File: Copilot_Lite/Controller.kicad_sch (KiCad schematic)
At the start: 36 parts, among them J11 SERIAL_MODE, J12 SERIAL_VOLTAGE_SELECT, Q5 BSS138, Q6 BSS138, Q7 BSS138, Q8 BSS138, U3 AP2204K-ADJ, U4 AP2204K-ADJ, U5 FT230XS, U6 TXB0104D

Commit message: lite: Replaced the old 'uCIme' name by the new 'Copilot' one in the board files.
Signed-off-by: Adrien Ricciardi <aricciardi@baylibre.com>
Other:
- title: uCIme Lite USB controller -> Copilot Lite USB controller

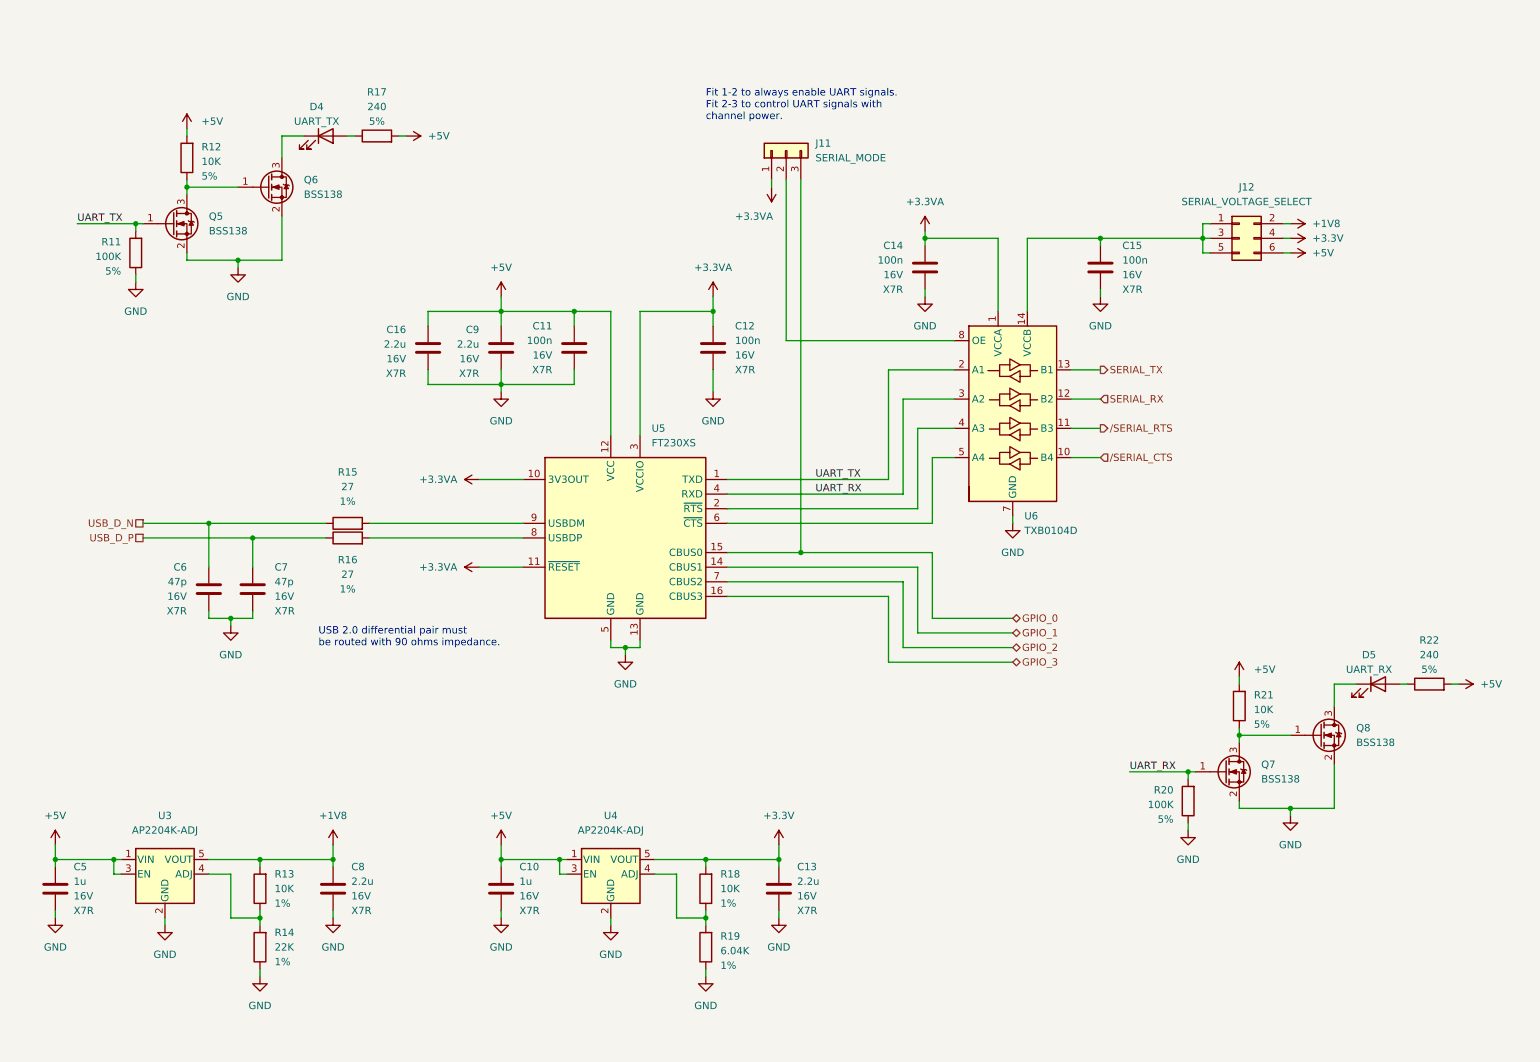
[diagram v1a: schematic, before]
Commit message: lite: Replaced the TXB0104 voltage translater by several SN74LV1T125.
The TXB0104 is not able to translate down to 1.8V on its Vccb supply side if the Vcca supply is 3.3V.

Signed-off-by: Adrien Ricciardi <aricciardi@baylibre.com>
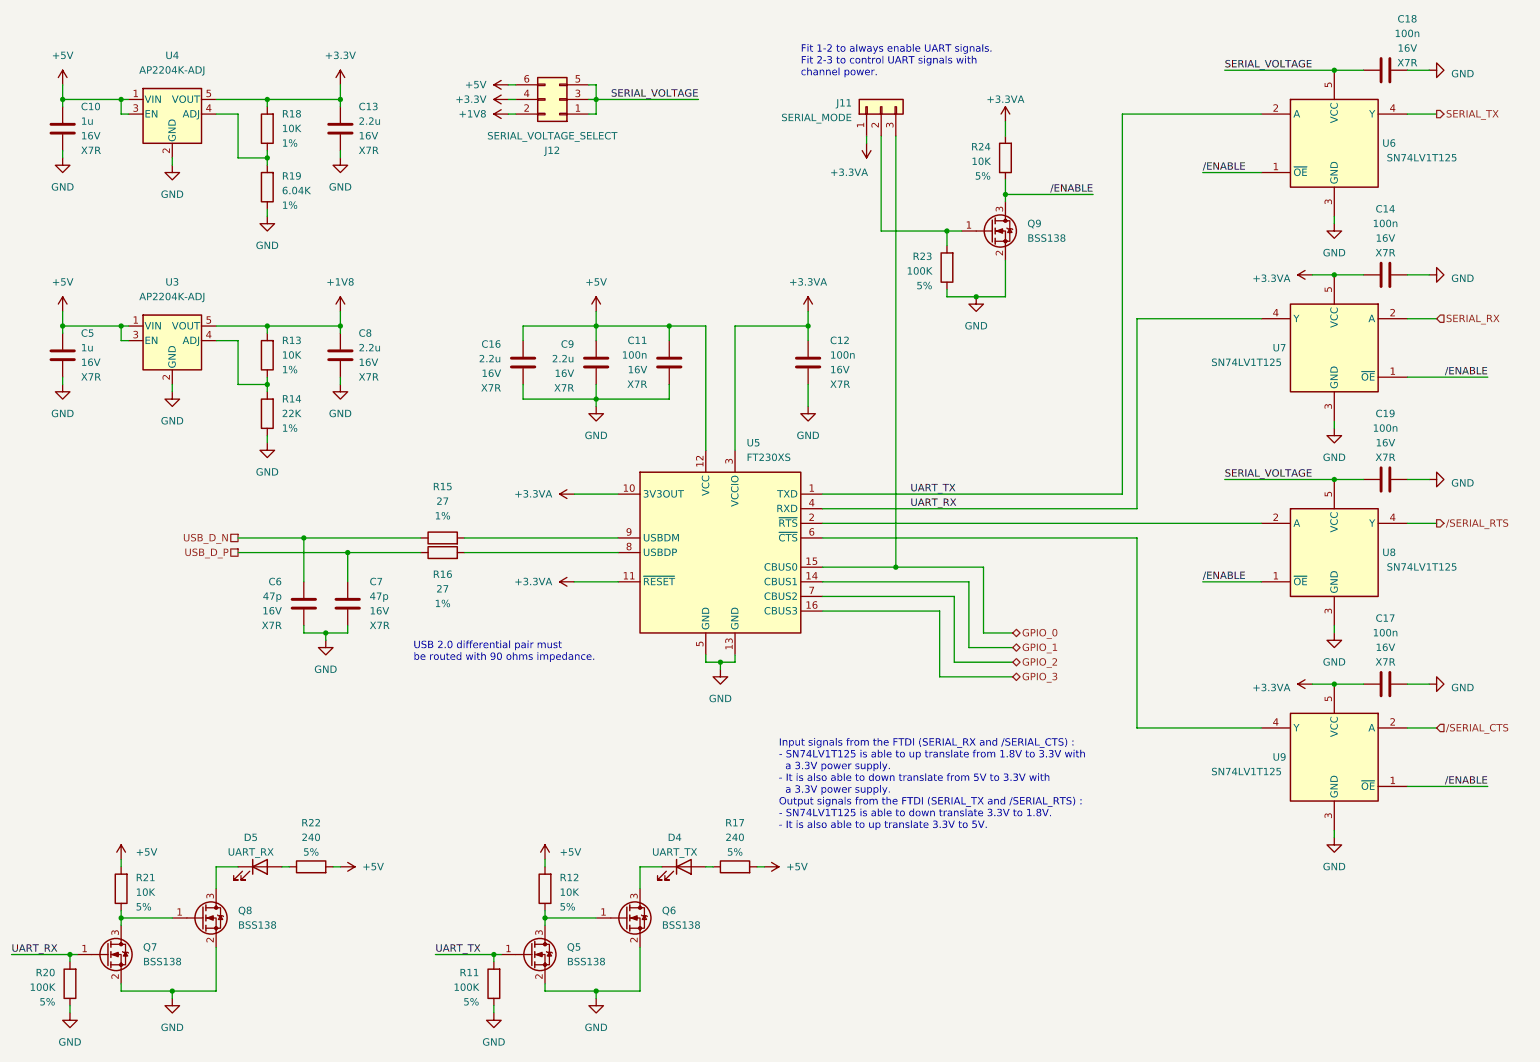
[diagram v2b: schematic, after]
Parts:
- removed C15: 100n, Capacitor_SMD:C_0603_1608Metric, symbol Device:C
- removed U6: TXB0104D, Package_SO:SOIC-14_3.9x8.7mm_P1.27mm, symbol Logic_LevelTranslator:TXB0104D
- added C17, C18, C19: 100n, Capacitor_SMD:C_0603_1608Metric, symbol Device:C
- added Q9: BSS138, Package_TO_SOT_SMD:SOT-23, symbol Transistor_FET:BSS138
- added R23: 100K, Resistor_SMD:R_0603_1608Metric, symbol Device:R
- added R24: 10K, Resistor_SMD:R_0603_1608Metric, symbol Device:R
- added U6, U7, U8, U9: SN74LV1T125, Package_TO_SOT_SMD:SOT-23-5, symbol SN74LV1T125:SN74LV1T125DBV
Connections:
- net +3.3VA: now also C17.1, R24.2, U7.5 (VCC), U9.5 (VCC)
- net GND: now also C17.2, C18.2, C19.2, Q9.2 (S), R23.1, U6.3 (GND), U7.3 (GND), U8.3 (GND), U9.3 (GND)
- net SERIAL_RX: now also U7.2 (A)
- net SERIAL_TX: now also U6.4 (Y)
- net UART_RX: now also U7.4 (Y)
- net UART_TX: now also U6.2 (A)
- net /SERIAL_CTS: now also U9.2 (A)
- net /SERIAL_RTS: now also U8.4 (Y)
- net SERIAL_VOLTAGE: now reaches J12.1 (Pin_1), J12.3 (Pin_3), J12.5 (Pin_5)
- net SERIAL_VOLTAGE: now also C18.1, C19.1, U6.5 (VCC), U8.5 (VCC)
- net at U5.2 (~{RTS}): now also U8.2 (A)
- net at U5.6 (~{CTS}): now also U9.4 (Y)
- net at J11.2 (Pin_2): now also Q9.1 (G), R23.2
- new net /ENABLE: Q9.3 (D), R24.1, U6.1 (~{OE}), U7.1 (~{OE}), U8.1 (~{OE}), U9.1 (~{OE})
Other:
- note added: "Input signals from the FTDI (SERIAL_RX and /SERIAL_CTS) : - SN74LV1T125 is able to up translate from 1.8V to 3.3V with a 3.3V power supply. - It is also able to down translate from 5V to 3.3V with a 3.3V power supply. Output signals from the FTDI (SERIAL_TX and /SERIAL_RTS) : - SN74LV1T125 is able to down translate 3.3V to 1.8V. - It is also able to up translate 3.3V to 5V."
- moved on the sheet: C10, C11, C12, C13, C14, C16, C5, C6, C7, C8, C9, D4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

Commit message: lite: Added the SN74LV1T125 part numbers to both schematic and PCB.
Signed-off-by: Adrien Ricciardi <aricciardi@baylibre.com>
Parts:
- U6, U7, U8, U9: AISLER_MPN (none) -> SN74LV1T125DBV; PartNumber (none) -> SN74LV1T125DBV
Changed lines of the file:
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@@
+      (effects (font (size 1.27 1.27)) hide)
+    )
+    (property "AISLER_MPN" "SN74LV1T125DBV" (at 248.92 142.24 0)
+      (effects (font (size 1.27 1.27)) hide)
+    )
+    (property "PartNumber" "SN74LV1T125DBV" (at 248.92 142.24 0)
       (effects (font (size 1.27 1.27)) hide)
     )
@@
       (effects (font (size 1.27 1.27)) hide)
     )
+    (property "AISLER_MPN" "SN74LV1T125DBV" (at 248.92 106.68 0)
+      (effects (font (size 1.27 1.27)) hide)
+    )
+    (property "PartNumber" "SN74LV1T125DBV" (at 248.92 106.68 0)
+      (effects (font (size 1.27 1.27)) hide)
+    )
     (pin "1")
     (pin "2")
@@
       (effects (font (size 1.27 1.27)) hide)
     )
+    (property "AISLER_MPN" "SN74LV1T125DBV" (at 248.92 35.56 0)
+      (effects (font (size 1.27 1.27)) hide)
+    )
+    (property "PartNumber" "SN74LV1T125DBV" (at 248.92 35.56 0)
+      (effects (font (size 1.27 1.27)) hide)
+    )
     (pin "1")
     (pin "2")
@@
       (effects (font (size 1.27 1.27)) hide)
     )
+    (property "AISLER_MPN" "SN74LV1T125DBV" (at 248.92 71.12 0)
+      (effects (font (size 1.27 1.27)) hide)
+    )
+    (property "PartNumber" "SN74LV1T125DBV" (at 248.92 71.12 0)
+      (effects (font (size 1.27 1.27)) hide)
+    )
